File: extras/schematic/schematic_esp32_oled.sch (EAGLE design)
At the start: 21 parts, among them U1 SI4735-D60-GU, U2 ESP32-DEVKITC-32D

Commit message: SI473X Arduino Library
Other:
- note added: "Optional"
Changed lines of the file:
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@@
 <text x="5.08" y="76.2" size="1.778" layer="91">If GND, I2C addr =  0x11</text>
 <text x="5.08" y="71.12" size="1.778" layer="91">If VCC, I2C addr =  0x63</text>
+<rectangle x1="-53.34" y1="157.48" x2="-38.1" y2="170.18" layer="205"/>
+<text x="-50.8" y="172.72" size="1.778" layer="205">Optional</text>
 </plain>
 <instances>

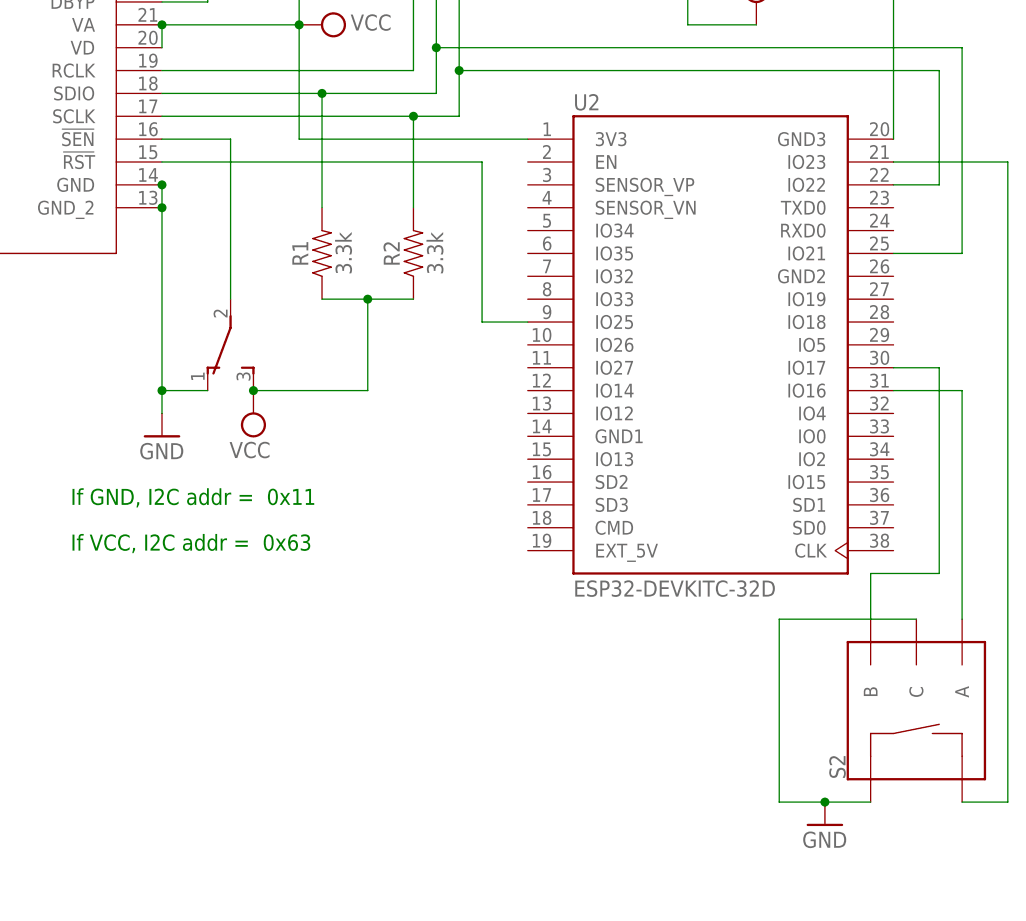
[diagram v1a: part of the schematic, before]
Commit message: SI473X Arduino Library
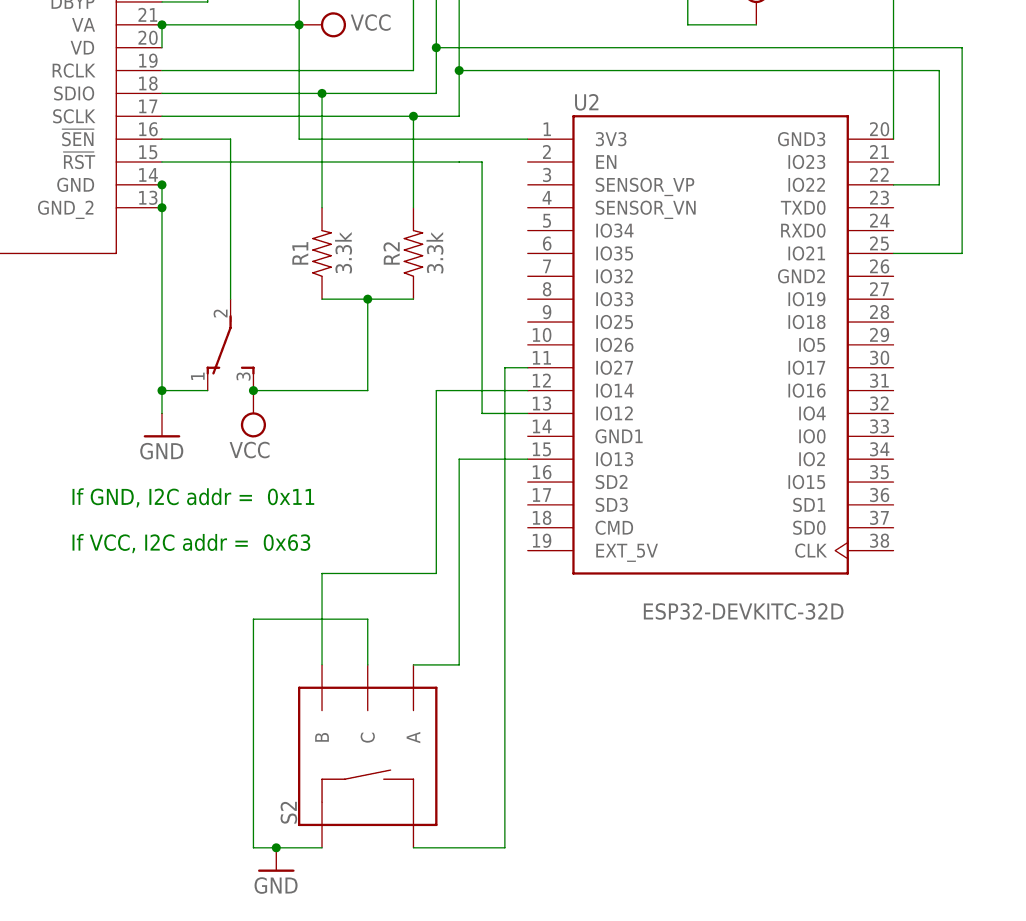
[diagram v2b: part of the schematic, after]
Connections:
- removed net N$20: S2.SW-, U2.IO23
- new net N$18: S2.A, U2.IO13
- net N$14: now also S2.SW-, U2.IO27; no longer S2.A, U2.IO16
- net N$16: now also U2.IO14; no longer U2.IO17
- net N$17: now also U2.IO12; no longer U2.IO25
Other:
- moved on the sheet: S2
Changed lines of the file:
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@@
 <instance part="U2" gate="G$1" x="76.2" y="93.98" smashed="yes">
 <attribute name="NAME" x="60.9428" y="120.0443" size="1.78" layer="95"/>
-<attribute name="VALUE" x="60.9437" y="66.0102" size="1.7799" layer="96"/>
+<attribute name="VALUE" x="68.5637" y="63.4702" size="1.7799" layer="96"/>
 </instance>
-<instance part="S2" gate="G$1" x="99.06" y="53.34" smashed="yes" rot="R90">
-<attribute name="NAME" x="91.186" y="45.72" size="1.778" layer="95" font="vector" rot="R90"/>
+<instance part="S2" gate="G$1" x="38.1" y="48.26" smashed="yes" rot="R90">
+<attribute name="NAME" x="30.226" y="40.64" size="1.778" layer="95" font="vector" rot="R90"/>
 </instance>
-<instance part="GND6" gate="1" x="88.9" y="40.64" smashed="yes">
-<attribute name="VALUE" x="86.36" y="38.1" size="1.778" layer="96"/>
+<instance part="GND6" gate="1" x="27.94" y="35.56" smashed="yes">
+<attribute name="VALUE" x="25.4" y="33.02" size="1.778" layer="96"/>
 </instance>
 </instances>
@@
 <pinref part="S2" gate="G$1" pin="SW+"/>
 <pinref part="GND6" gate="1" pin="GND"/>
-<wire x1="93.98" y1="43.18" x2="88.9" y2="43.18" width="0.1524" layer="91"/>
-<wire x1="88.9" y1="43.18" x2="83.82" y2="43.18" width="0.1524" layer="91"/>
+<wire x1="33.02" y1="38.1" x2="27.94" y2="38.1" width="0.1524" layer="91"/>
 <pinref part="S2" gate="G$1" pin="C"/>
-<wire x1="99.06" y1="63.5" x2="83.82" y2="63.5" width="0.1524" layer="91"/>
-<wire x1="83.82" y1="63.5" x2="83.82" y2="43.18" width="0.1524" layer="91"/>
-<junction x="88.9" y="43.18"/>
+<wire x1="38.1" y1="58.42" x2="38.1" y2="63.5" width="0.1524" layer="91"/>
+<wire x1="38.1" y1="63.5" x2="25.4" y2="63.5" width="0.1524" layer="91"/>
+<wire x1="25.4" y1="63.5" x2="25.4" y2="38.1" width="0.1524" layer="91"/>
+<wire x1="25.4" y1="38.1" x2="27.94" y2="38.1" width="0.1524" layer="91"/>
+<junction x="27.94" y="38.1"/>
 </segment>
 </net>
@@
 <segment>
 <pinref part="U1" gate="A" pin="!RST"/>
-<wire x1="15.24" y1="114.3" x2="50.8" y2="114.3" width="0.1524" layer="91"/>
-<wire x1="50.8" y1="114.3" x2="50.8" y2="96.52" width="0.1524" layer="91"/>
-<pinref part="U2" gate="G$1" pin="IO25"/>
-<wire x1="50.8" y1="96.52" x2="55.88" y2="96.52" width="0.1524" layer="91"/>
+<wire x1="15.24" y1="114.3" x2="48.26" y2="114.3" width="0.1524" layer="91"/>
+<pinref part="U2" gate="G$1" pin="IO12"/>
+<wire x1="55.88" y1="86.36" x2="50.8" y2="86.36" width="0.1524" layer="91"/>
+<wire x1="50.8" y1="86.36" x2="50.8" y2="114.3" width="0.1524" layer="91"/>
+<wire x1="50.8" y1="114.3" x2="48.26" y2="114.3" width="0.1524" layer="91"/>
 </segment>
 </net>
@@
 <net name="N$14" class="0">
 <segment>
-<pinref part="U2" gate="G$1" pin="IO16"/>
-<wire x1="96.52" y1="88.9" x2="104.14" y2="88.9" width="0.1524" layer="91"/>
+<pinref part="S2" gate="G$1" pin="SW-"/>
+<pinref part="U2" gate="G$1" pin="IO27"/>
+<wire x1="55.88" y1="91.44" x2="53.34" y2="91.44" width="0.1524" layer="91"/>
+<wire x1="53.34" y1="91.44" x2="53.34" y2="38.1" width="0.1524" layer="91"/>
+<wire x1="43.18" y1="38.1" x2="53.34" y2="38.1" width="0.1524" layer="91"/>
+</segment>
+</net>
+<net name="N$16" class="0">
+<segment>
+<pinref part="U2" gate="G$1" pin="IO14"/>
+<wire x1="55.88" y1="88.9" x2="45.72" y2="88.9" width="0.1524" layer="91"/>
+<wire x1="45.72" y1="88.9" x2="45.72" y2="68.58" width="0.1524" layer="91"/>
+<wire x1="45.72" y1="68.58" x2="33.02" y2="68.58" width="0.1524" layer="91"/>
+<pinref part="S2" gate="G$1" pin="B"/>
+<wire x1="33.02" y1="68.58" x2="33.02" y2="58.42" width="0.1524" layer="91"/>
+</segment>
+</net>
+<net name="N$18" class="0">
+<segment>
+<pinref part="U2" gate="G$1" pin="IO13"/>
+<wire x1="55.88" y1="81.28" x2="48.26" y2="81.28" width="0.1524" layer="91"/>
+<wire x1="48.26" y1="81.28" x2="48.26" y2="58.42" width="0.1524" layer="91"/>
 <pinref part="S2" gate="G$1" pin="A"/>
-<wire x1="104.14" y1="88.9" x2="104.14" y2="63.5" width="0.1524" layer="91"/>
-</segment>
-</net>
-<net name="N$16" class="0">
-<segment>
-<pinref part="U2" gate="G$1" pin="IO17"/>
-<wire x1="96.52" y1="91.44" x2="101.6" y2="91.44" width="0.1524" layer="91"/>
-<wire x1="101.6" y1="91.44" x2="101.6" y2="68.58" width="0.1524" layer="91"/>
-<wire x1="101.6" y1="68.58" x2="93.98" y2="68.58" width="0.1524" layer="91"/>
-<pinref part="S2" gate="G$1" pin="B"/>
-<wire x1="93.98" y1="68.58" x2="93.98" y2="63.5" width="0.1524" layer="91"/>
-</segment>
-</net>
-<net name="N$20" class="0">
-<segment>
-<pinref part="S2" gate="G$1" pin="SW-"/>
-<wire x1="104.14" y1="43.18" x2="109.22" y2="43.18" width="0.1524" layer="91"/>
-<pinref part="U2" gate="G$1" pin="IO23"/>
-<wire x1="109.22" y1="43.18" x2="109.22" y2="114.3" width="0.1524" layer="91"/>
-<wire x1="109.22" y1="114.3" x2="96.52" y2="114.3" width="0.1524" layer="91"/>
-</segment>
-</net>
+<wire x1="48.26" y1="58.42" x2="43.18" y2="58.42" width="0.1524" layer="91"/>
+</segment>
+</net>
